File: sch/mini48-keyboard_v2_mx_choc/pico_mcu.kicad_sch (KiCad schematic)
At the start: 1 part, among them U2 Pico

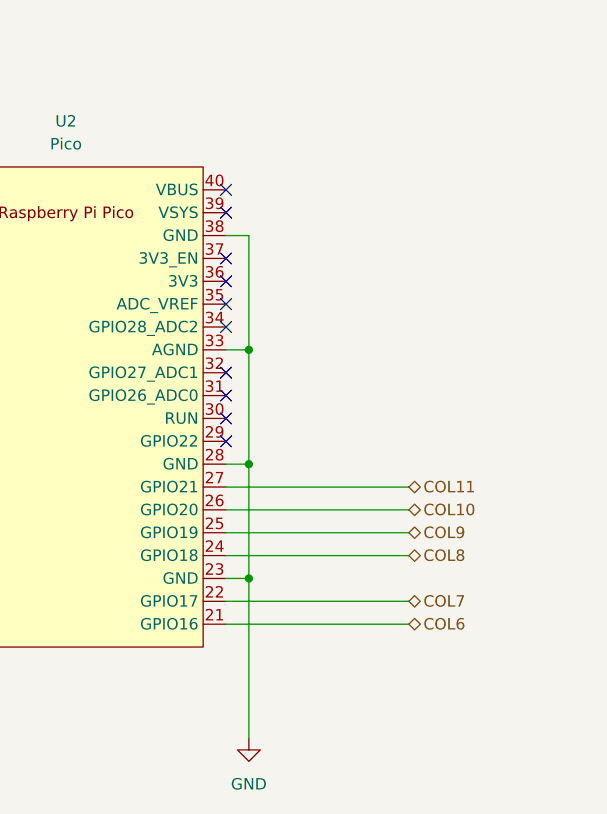
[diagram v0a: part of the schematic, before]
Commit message: ひとまずすべての未配線をなくした版です。 配線は整えていません。 また、GNDプレーンのビアは打っていません。
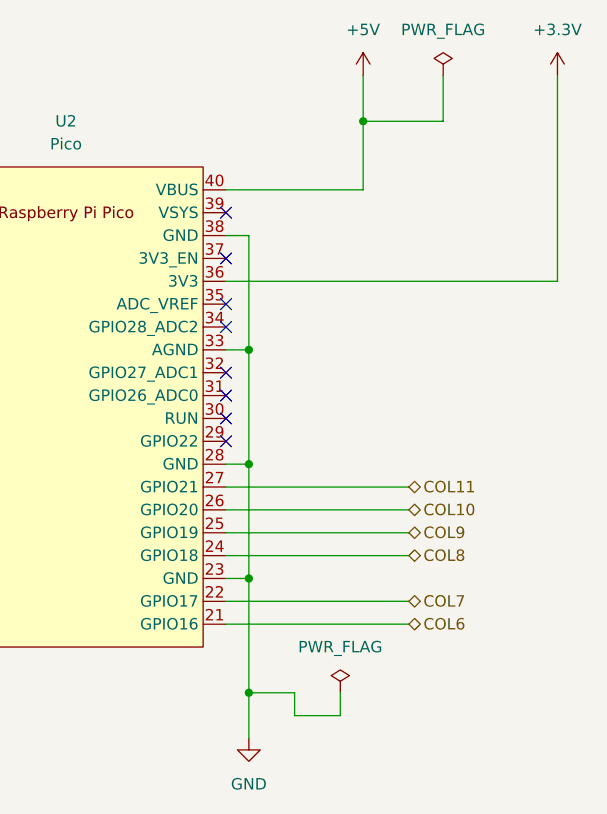
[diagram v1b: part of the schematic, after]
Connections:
- net +3.3V: now reaches U2.36 (3V3)
- net +5V: now reaches U2.40 (VBUS)
- no-connect marks 13 -> 11

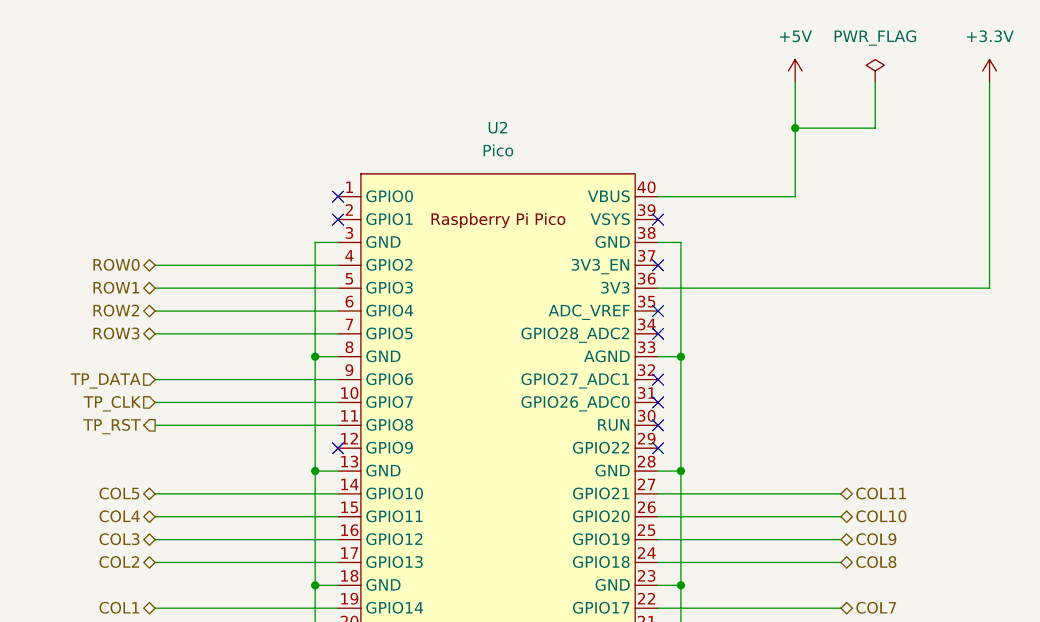
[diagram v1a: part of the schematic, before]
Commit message: トラックポイント(2ピースタイプ)の取り付けステーです。 トラックポイントの軸の延長部品です。
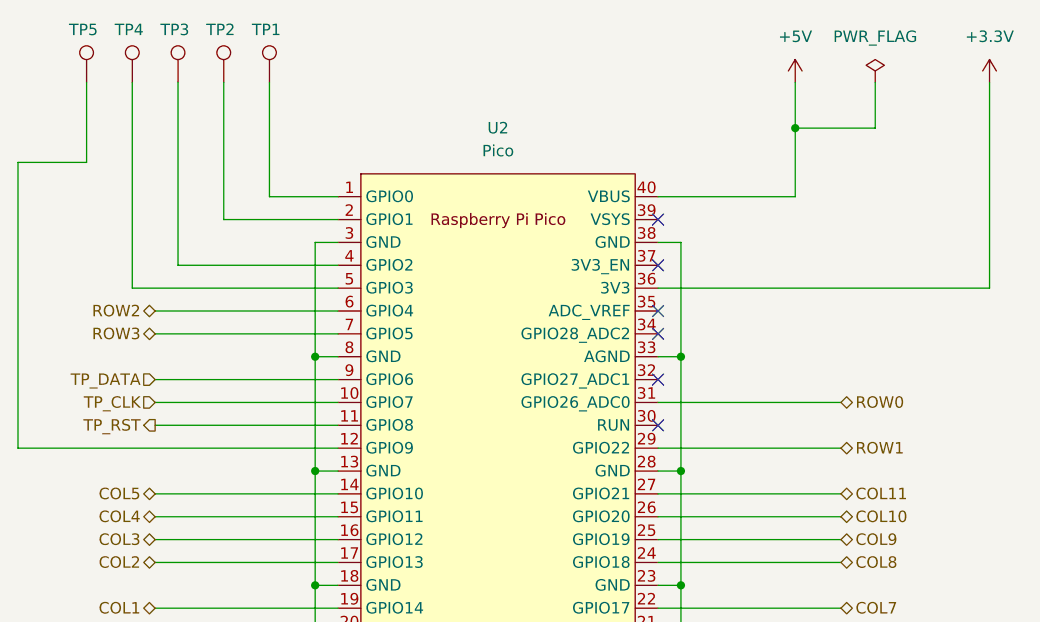
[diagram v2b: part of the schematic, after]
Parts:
- added TP1, TP2, TP3, TP4, TP5: TestPoint, TestPoint:TestPoint_Pad_D1.0mm, symbol Connector:TestPoint
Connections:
- net ROW0: now also U2.31 (GPIO26_ADC0); no longer U2.4 (GPIO2)
- net ROW1: now also U2.29 (GPIO22); no longer U2.5 (GPIO3)
- net at U2.1 (GPIO0): now also TP1.1
- net at U2.12 (GPIO9): now also TP5.1
- net at U2.2 (GPIO1): now also TP2.1
- new net: TP4.1, U2.5 (GPIO3)
- new net: TP3.1, U2.4 (GPIO2)
- no-connect marks 11 -> 6

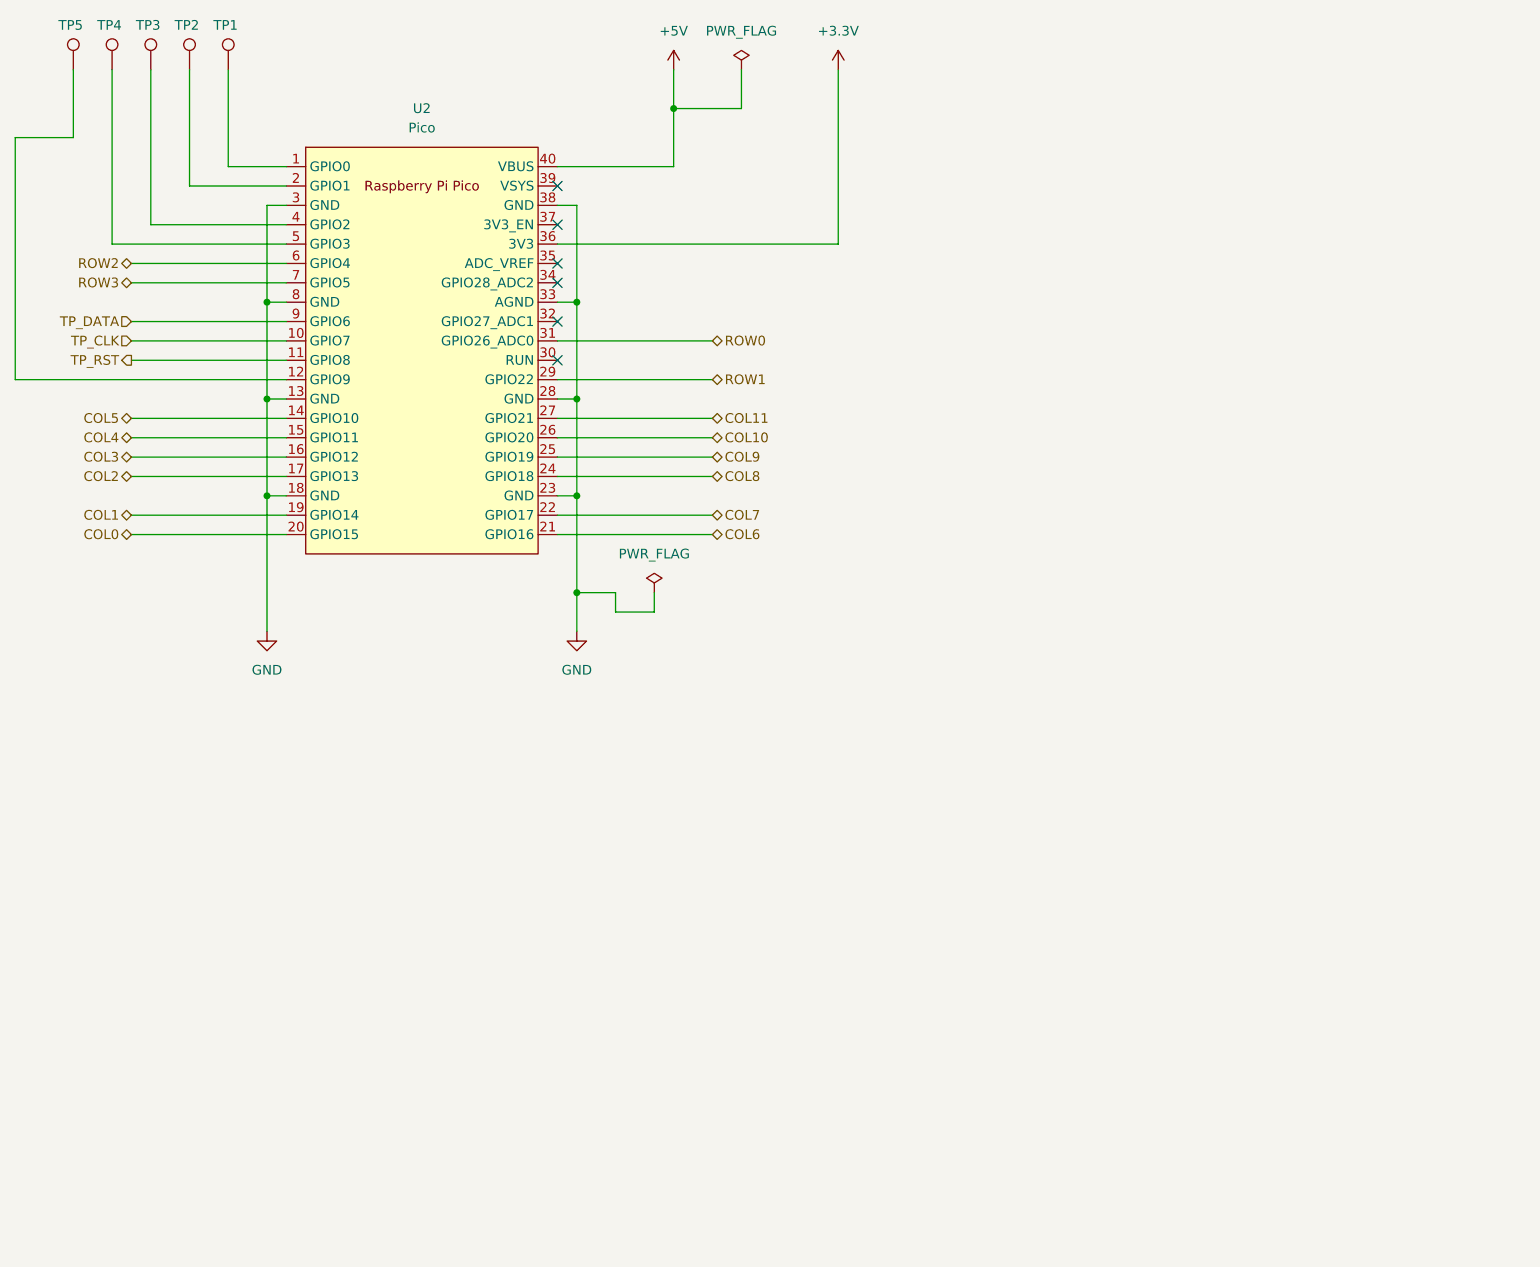
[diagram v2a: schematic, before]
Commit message: picoの位置を左上に変更しました。
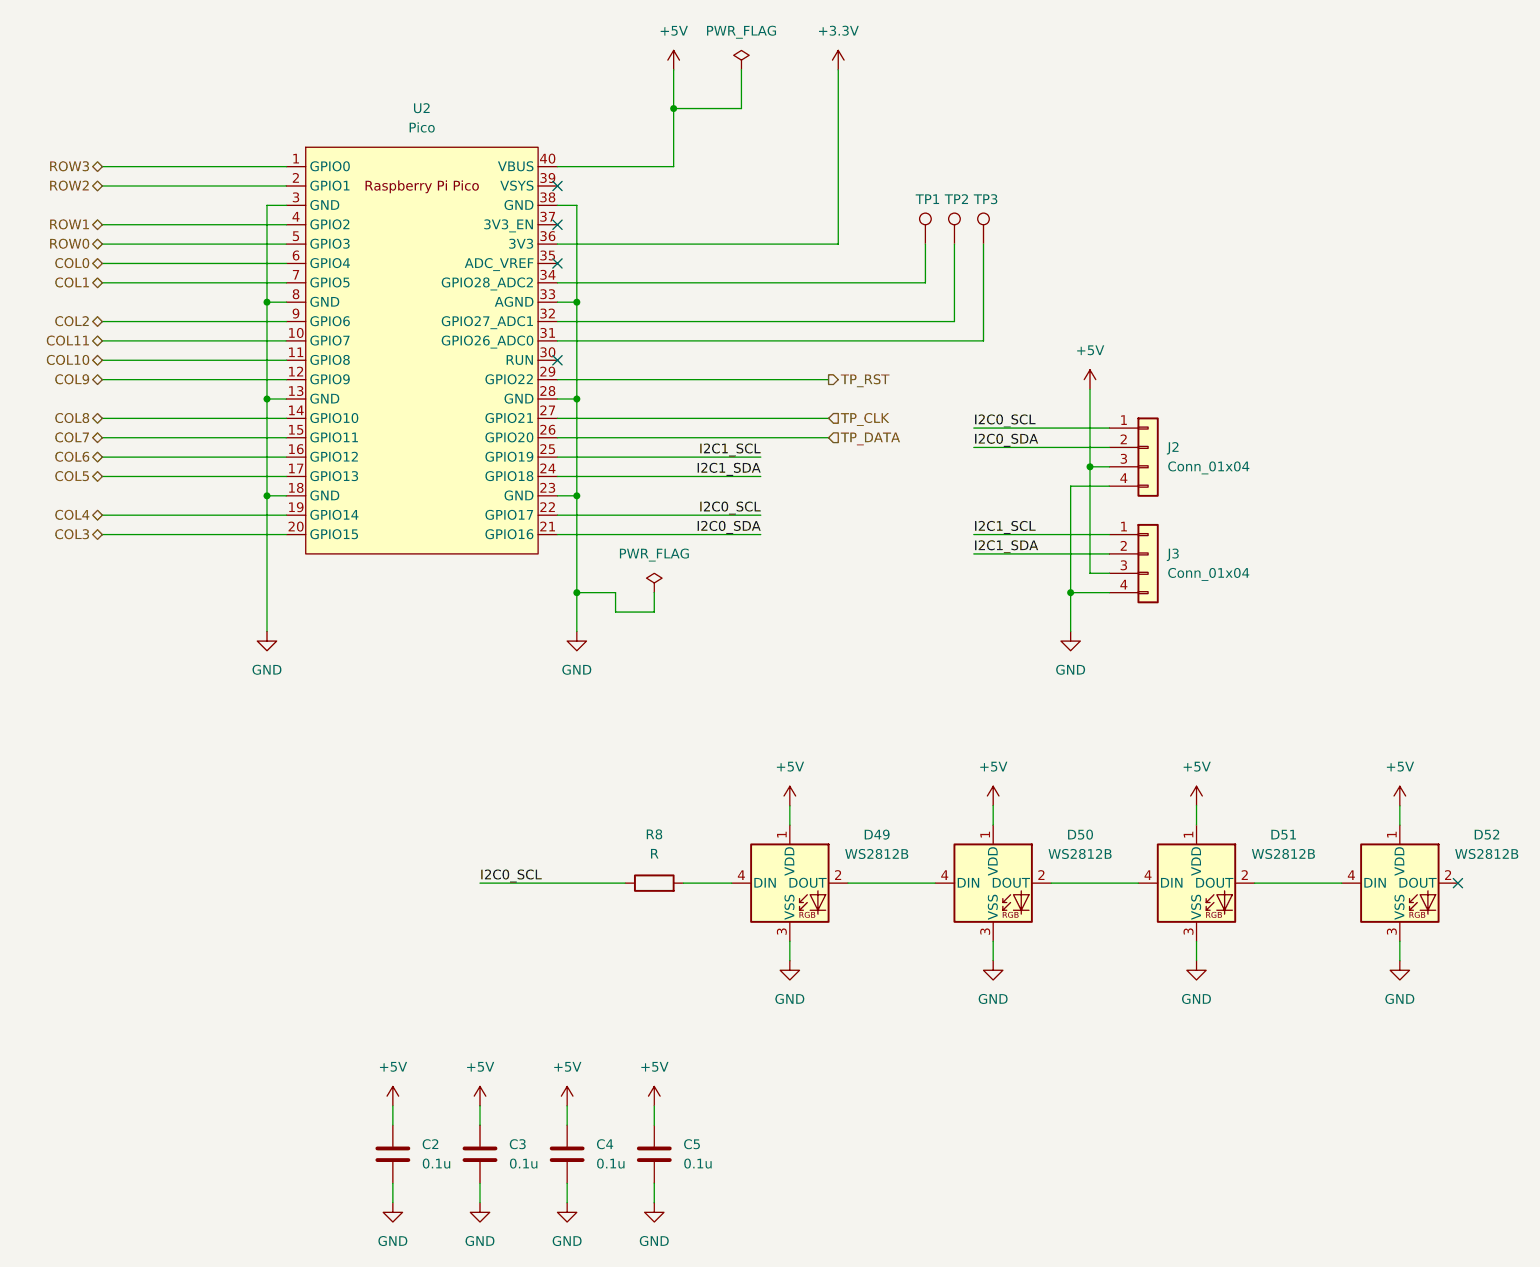
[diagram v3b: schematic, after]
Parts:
- removed TP4, TP5: TestPoint, TestPoint:TestPoint_Pad_D1.0mm, symbol Connector:TestPoint
- added C2, C3, C4, C5: 0.1u, Capacitor_SMD:C_0603_1608Metric, symbol Device:C
- added D49, D50, D51, D52: WS2812B, LED_SMD:LED_WS2812B_PLCC4_5.0x5.0mm_P3.2mm, symbol LED:WS2812B
- added J2, J3: Conn_01x04, Connector_JST:JST_PH_S4B-PH-K_1x04_P2.00mm_Horizontal, symbol Connector_Generic:Conn_01x04
- added R8: R, Resistor_SMD:R_0603_1608Metric, symbol Device:R
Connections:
- net +5V: now also C2.1, C3.1, C4.1, C5.1, D49.1 (VDD), D50.1 (VDD), D51.1 (VDD), D52.1 (VDD), J2.3 (Pin_3), J3.3 (Pin_3)
- net COL0: now also U2.6 (GPIO4); no longer U2.20 (GPIO15)
- net COL1: now also U2.7 (GPIO5); no longer U2.19 (GPIO14)
- net COL10: now also U2.11 (GPIO8); no longer U2.26 (GPIO20)
- net COL11: now also U2.10 (GPIO7); no longer U2.27 (GPIO21)
- net COL2: now also U2.9 (GPIO6); no longer U2.17 (GPIO13)
- net COL3: now also U2.20 (GPIO15); no longer U2.16 (GPIO12)
- net COL4: now also U2.19 (GPIO14); no longer U2.15 (GPIO11)
- net COL5: now also U2.17 (GPIO13); no longer U2.14 (GPIO10)
- net COL6: now also U2.16 (GPIO12); no longer U2.21 (GPIO16)
- net COL7: now also U2.15 (GPIO11); no longer U2.22 (GPIO17)
- net COL8: now also U2.14 (GPIO10); no longer U2.24 (GPIO18)
- net COL9: now also U2.12 (GPIO9); no longer U2.25 (GPIO19)
- net GND: now also C2.2, C3.2, C4.2, C5.2, D49.3 (VSS), D50.3 (VSS), D51.3 (VSS), D52.3 (VSS), J2.4 (Pin_4), J3.4 (Pin_4)
- net ROW0: now also U2.5 (GPIO3); no longer U2.31 (GPIO26_ADC0)
- net ROW1: now also U2.4 (GPIO2); no longer U2.29 (GPIO22)
- net ROW2: now also U2.2 (GPIO1); no longer U2.6 (GPIO4)
- net ROW3: now also U2.1 (GPIO0); no longer U2.7 (GPIO5)
- net TP_CLK: now also U2.27 (GPIO21); no longer U2.10 (GPIO7)
- net TP_DATA: now also U2.26 (GPIO20); no longer U2.9 (GPIO6)
- net TP_RST: now also U2.29 (GPIO22); no longer U2.11 (GPIO8)
- net at TP2.1: now also U2.32 (GPIO27_ADC1); no longer U2.2 (GPIO1)
- net at TP3.1: now also U2.31 (GPIO26_ADC0); no longer U2.4 (GPIO2)
- net at TP1.1: now also U2.34 (GPIO28_ADC2); no longer U2.1 (GPIO0)
- new net: D50.2 (DOUT), D51.4 (DIN)
- new net: D49.2 (DOUT), D50.4 (DIN)
- new net: D51.2 (DOUT), D52.4 (DIN)
- new net: D49.4 (DIN), R8.2
- new net I2C0_SCL: J2.1 (Pin_1), R8.1, U2.22 (GPIO17)
- new net I2C0_SDA: J2.2 (Pin_2), U2.21 (GPIO16)
- new net I2C1_SCL: J3.1 (Pin_1), U2.25 (GPIO19)
- new net I2C1_SDA: J3.2 (Pin_2), U2.24 (GPIO18)
- no-connect marks 6 -> 5
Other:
- moved on the sheet: TP1
